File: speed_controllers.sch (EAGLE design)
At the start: 18 parts

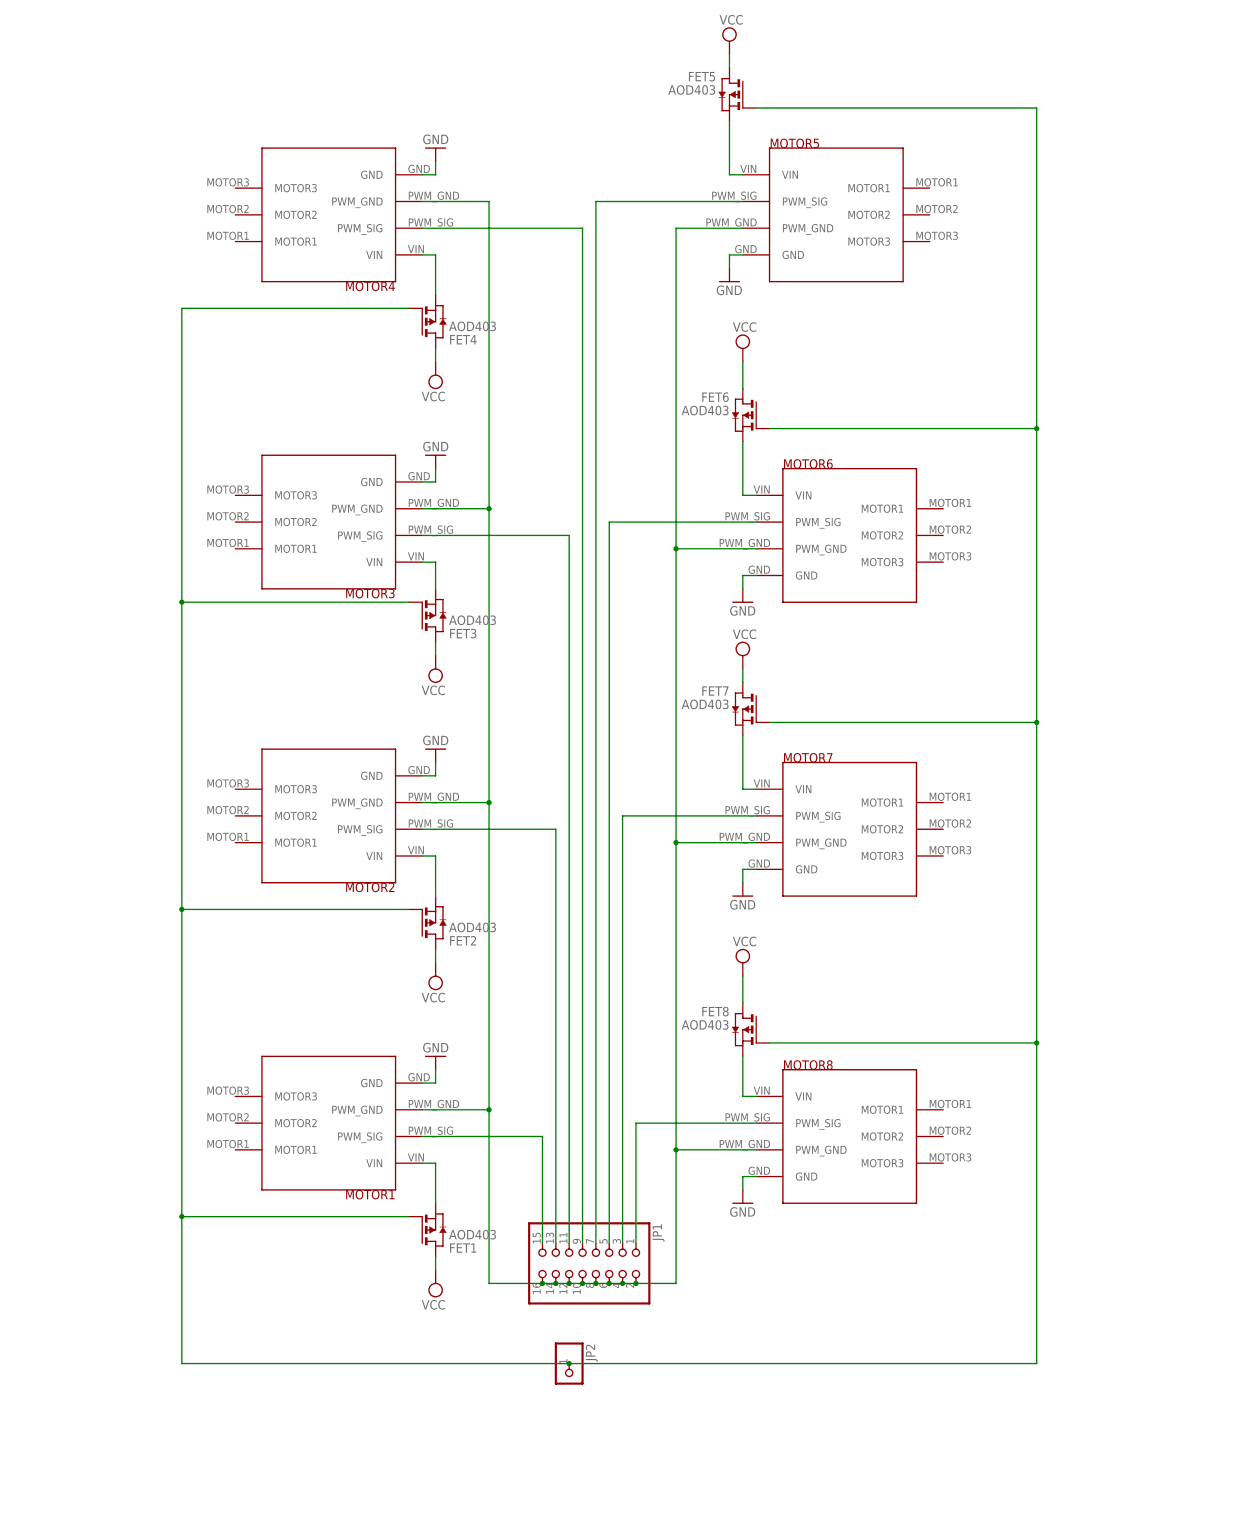
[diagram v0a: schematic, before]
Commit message: Redone ESC boards
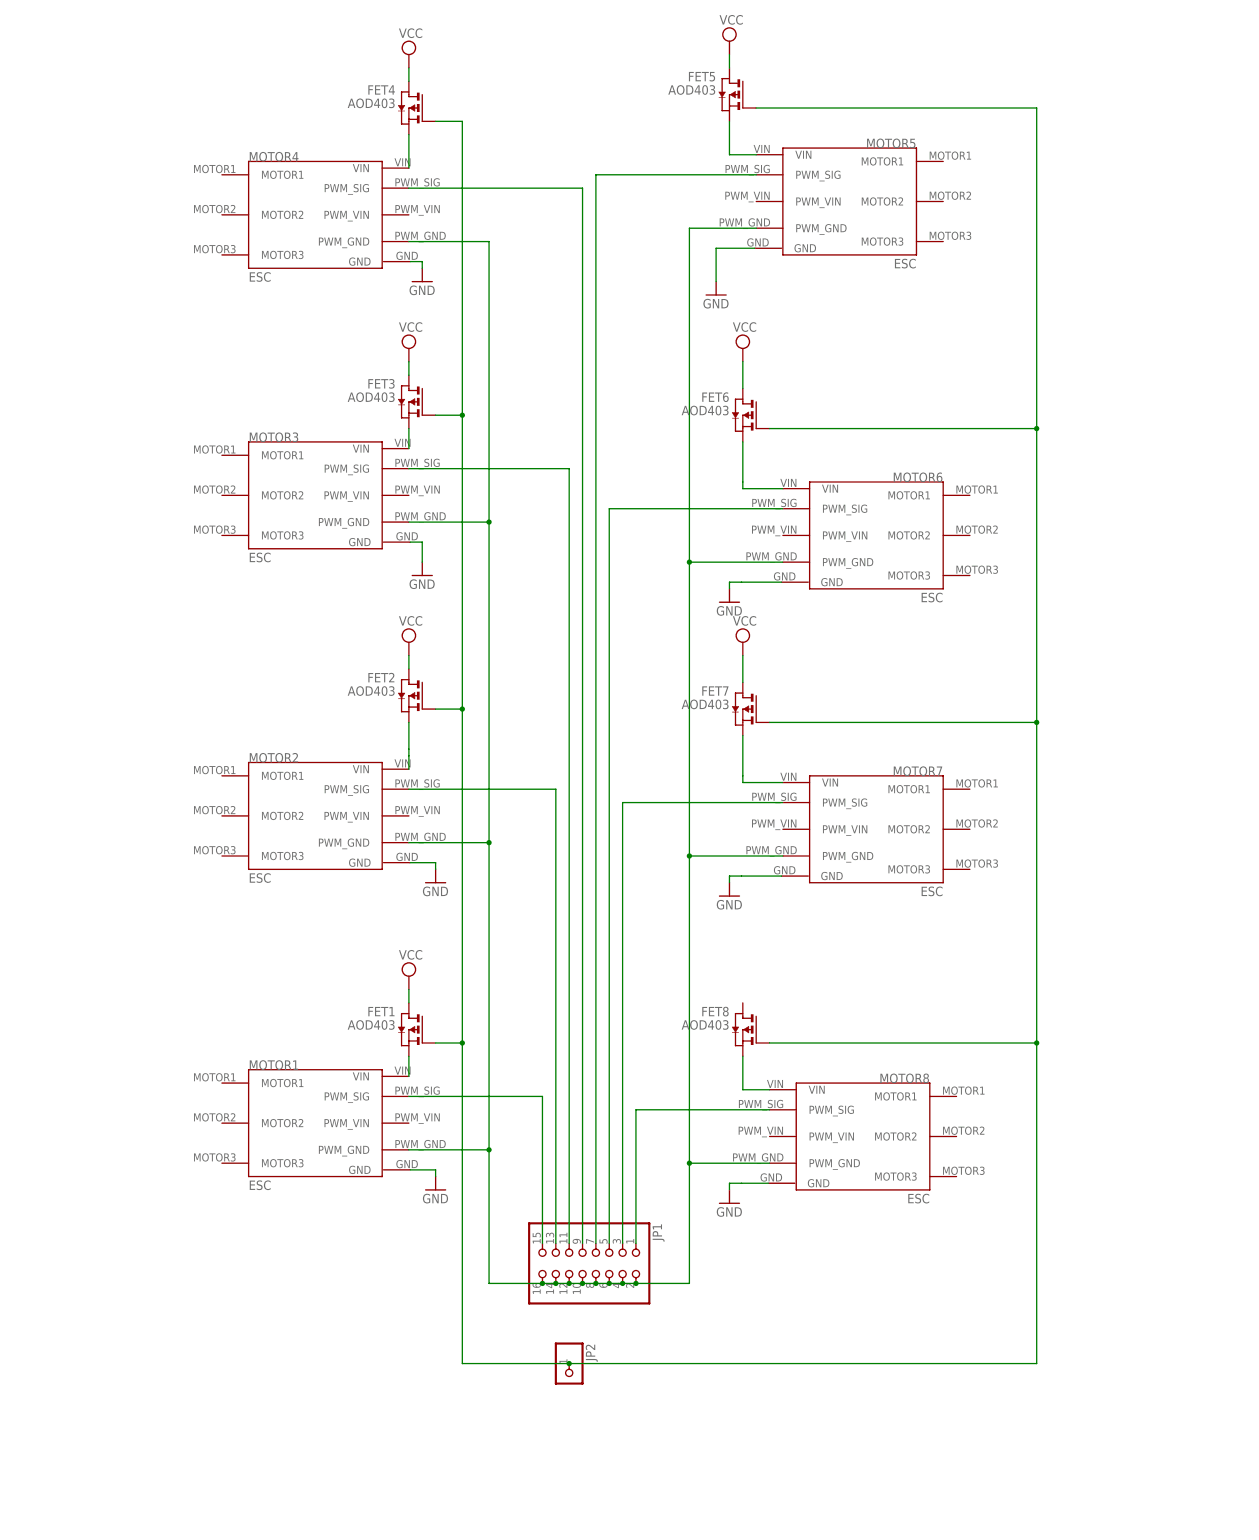
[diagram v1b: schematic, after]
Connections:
- net VCC: no longer FET8.D
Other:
- moved on the sheet: FET1, FET2, FET3, FET4

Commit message: Fixed everything in issue Redone ESC boards #2
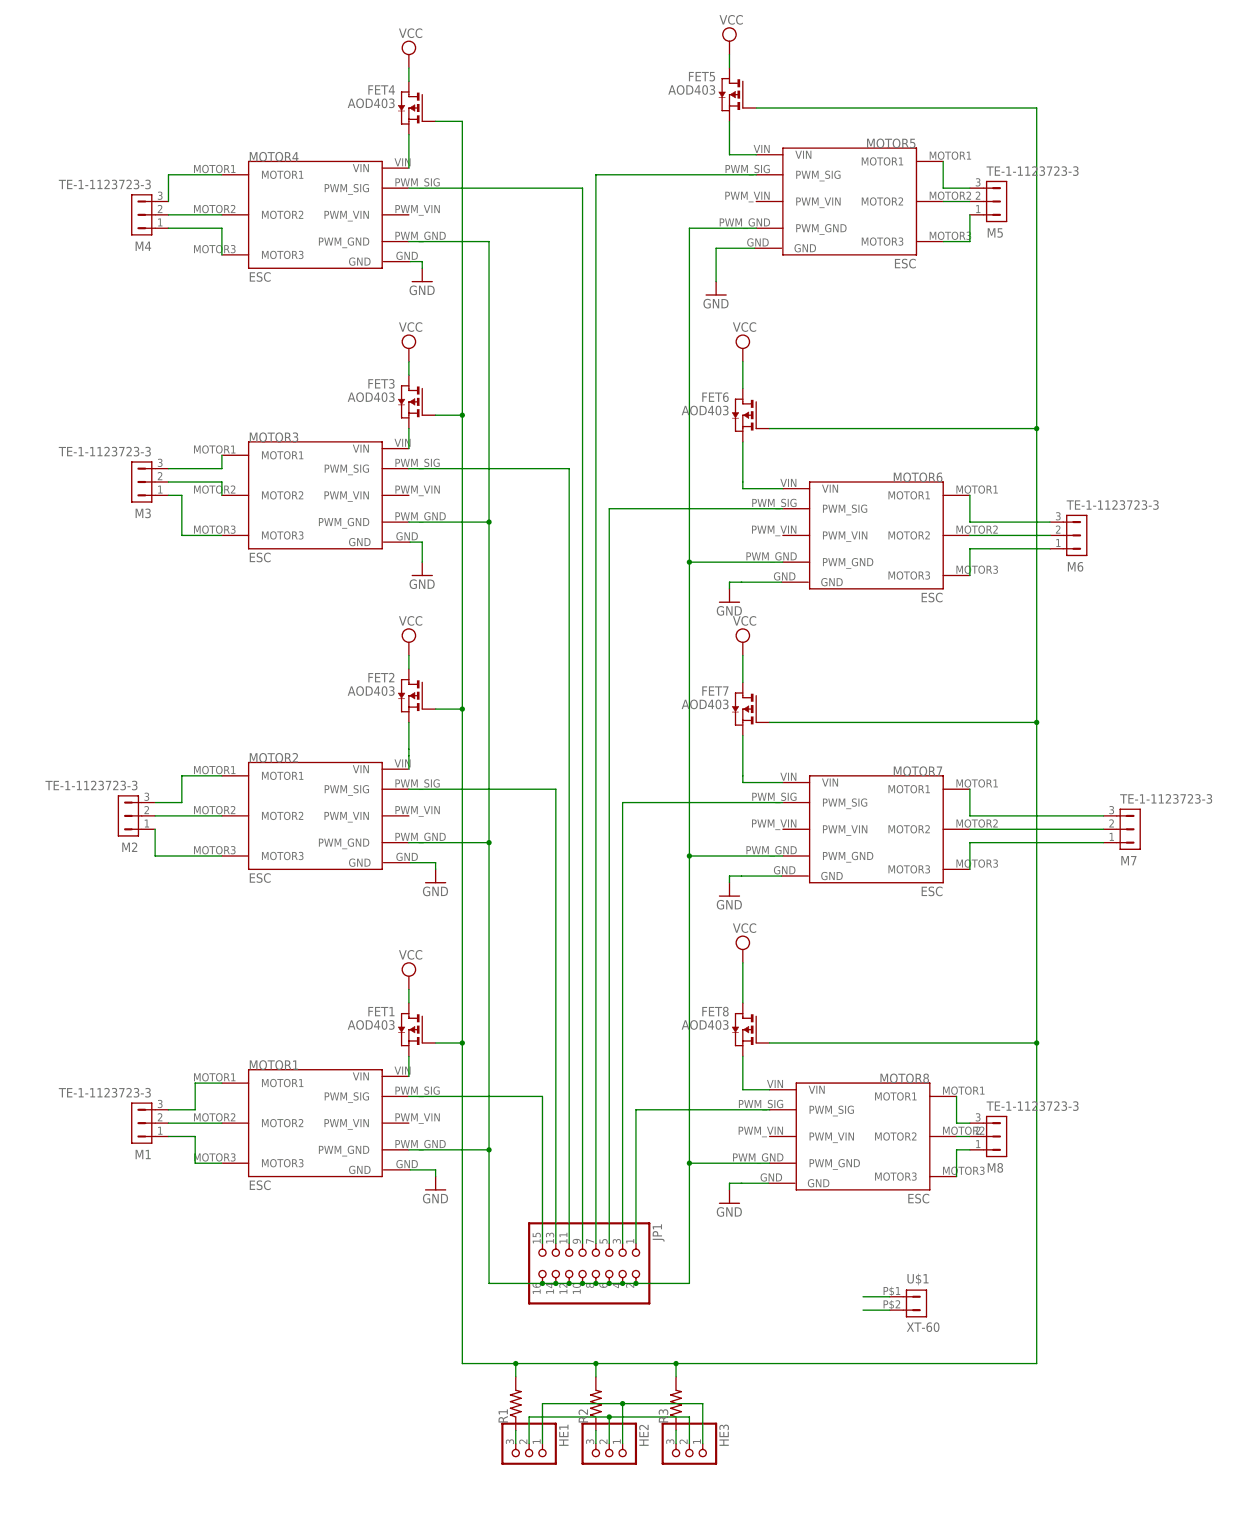
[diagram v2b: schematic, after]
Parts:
- removed JP2: (no value), auv:PINHD-1X1
- added HE1, HE2, HE3: (no value), auv:PINHD-1X3
- added M1, M2, M3, M4, M5, M6, M7, M8: TE-1-1123723-3, auv:TE-1-1123723-3
- added R1, R2, R3: (no value), auv:R-US_R0603
- added U$1: XT-60, auv:XT-60
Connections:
- net N$1 renamed SIG_6
- net N$10 renamed SIG_3
- net N$11 renamed SIG_2
- net N$12 renamed SIG_7
- net N$13 renamed SIG_8
- net N$14 renamed SIG_1
- net N$15 renamed VIN_2
- net N$16 renamed VIN3
- net N$17 renamed VIN_4
- net N$18 renamed VIN_8
- net N$2 renamed PWM_GND
- net N$3 renamed VIN_1
- net N$4 renamed SIG_5
- net N$5 renamed VIN_5
- net N$6 renamed SIG_4
- net N$8 renamed VIN_7
- net N$9 renamed VIN_6
- removed net N$20: FET1.G, FET2.G, FET3.G, FET4.G, FET5.G, FET6.G, FET7.G, FET8.G, JP2.1
- new net FET_G: FET1.G, FET2.G, FET3.G, FET4.G, FET5.G, FET6.G, FET7.G, FET8.G, R1.2, R2.2, R3.2
- new net M1_1: M1.1, MOTOR1.MOTOR3
- new net M1_2: M1.2, MOTOR1.MOTOR2
- new net M1_3: M1.3, MOTOR1.MOTOR1
- new net M2_1: M2.1, MOTOR2.MOTOR3
- new net M2_2: M2.2, MOTOR2.MOTOR2
- new net M2_3: M2.3, MOTOR2.MOTOR1
- new net M3_1: M3.1, MOTOR3.MOTOR3
- new net M3_2: M3.2, MOTOR3.MOTOR2
- new net M3_3: M3.3, MOTOR3.MOTOR1
- new net M4_1: M4.1, MOTOR4.MOTOR3
- new net M4_2: M4.2, MOTOR4.MOTOR2
- new net M4_3: M4.3, MOTOR4.MOTOR1
- new net M5_1: M5.1, MOTOR5.MOTOR3
- new net M5_2: M5.2, MOTOR5.MOTOR2
- new net M5_3: M5.3, MOTOR5.MOTOR1
- new net M6_1: M6.1, MOTOR6.MOTOR3
- new net M6_2: M6.2, MOTOR6.MOTOR2
- new net M6_3: M6.3, MOTOR6.MOTOR1
- new net M7_1: M7.1, MOTOR7.MOTOR3
- new net M7_2: M7.2, MOTOR7.MOTOR2
- new net M7_3: M7.3, MOTOR7.MOTOR1
- new net M8_1: M8.1, MOTOR8.MOTOR3
- new net M8_2: M8.2, MOTOR8.MOTOR2
- new net M8_3: M8.3, MOTOR8.MOTOR1
- new net N$4: HE1.3, R1.1
- new net N$5: HE2.3, R2.1
- new net N$6: HE3.3, R3.1
- net GND: now also HE1.2, HE2.2, HE3.2, U$1.2
- net VCC: now also FET8.D, HE1.1, HE2.1, HE3.1, U$1.1

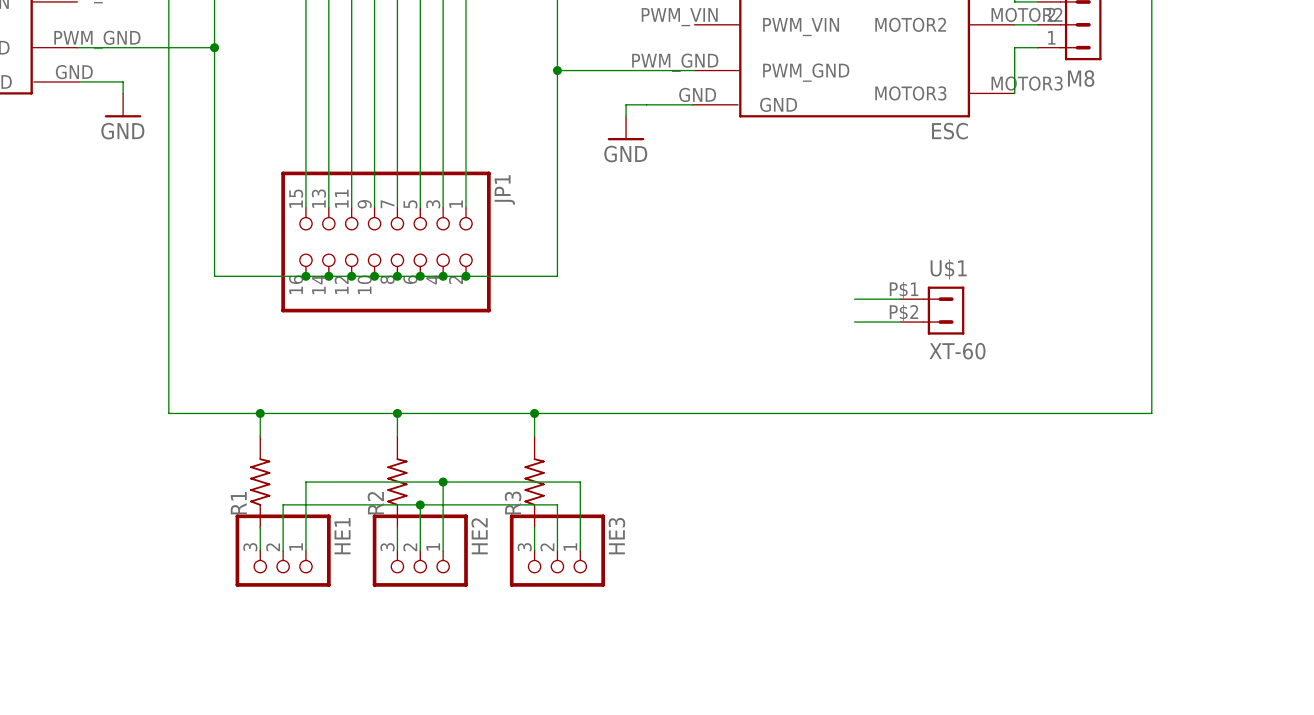
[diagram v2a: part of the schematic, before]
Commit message: Added Optocoupler and Hall effect sensors
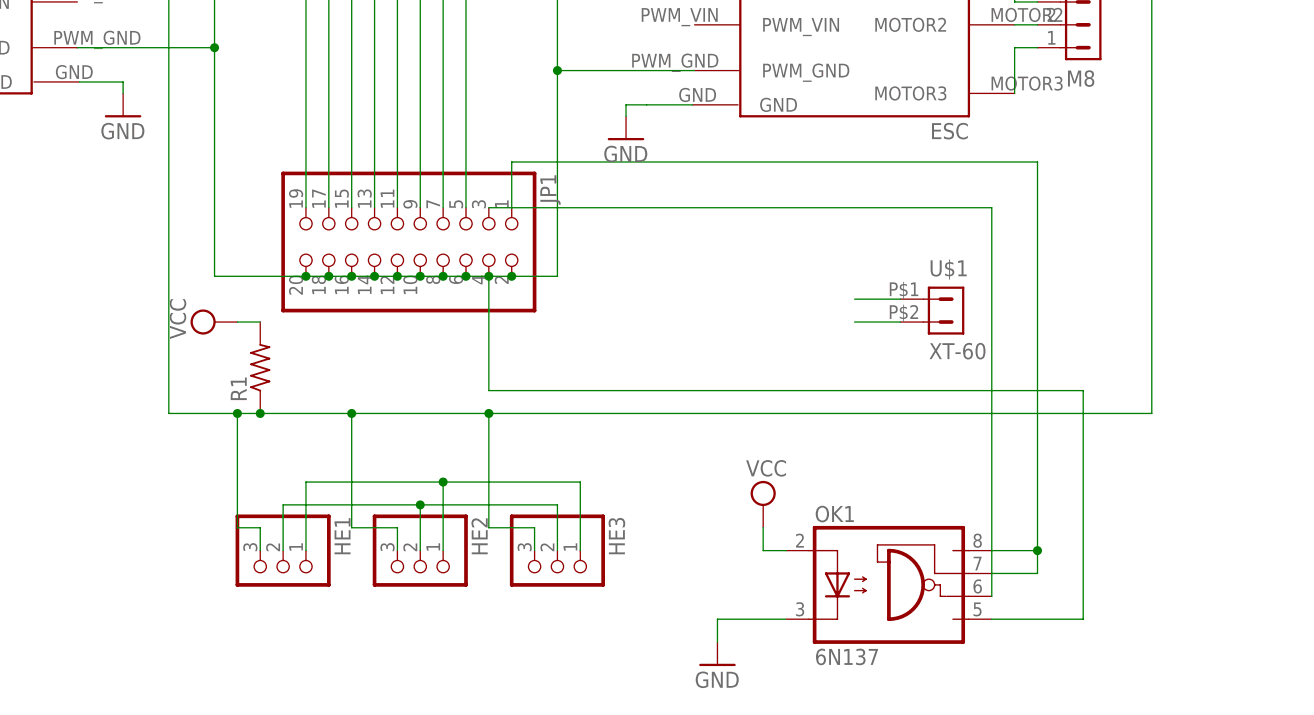
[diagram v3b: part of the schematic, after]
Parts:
- removed R2, R3: (no value), auv:R-US_R0603
- added OK1: 6N137, auv:6N137
- JP1: device auv:PINHD-2X8 -> auv:PINHD-2X10
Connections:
- removed net N$6: HE3.3, R3.1
- net FET_G: now also HE1.3, HE2.3, HE3.3, R1.1; no longer R1.2, R2.2, R3.2
- net GND: now also OK1.C
- net N$4: now also JP1.1, OK1.VCC, OK1.VE; no longer HE1.3, R1.1
- net N$5: now also JP1.3, OK1.VO; no longer HE2.3, R2.1
- net PWM_GND: now also JP1.18, JP1.20, OK1.GND
- net SIG_1: now also JP1.19; no longer JP1.15
- net SIG_2: now also JP1.17; no longer JP1.13
- net SIG_3: now also JP1.15; no longer JP1.11
- net SIG_4: now also JP1.13; no longer JP1.9
- net SIG_5: now also JP1.11; no longer JP1.7
- net SIG_6: now also JP1.9; no longer JP1.5
- net SIG_7: now also JP1.7; no longer JP1.3
- net SIG_8: now also JP1.5; no longer JP1.1
- net VCC: now also OK1.A, R1.2
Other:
- moved on the sheet: R1

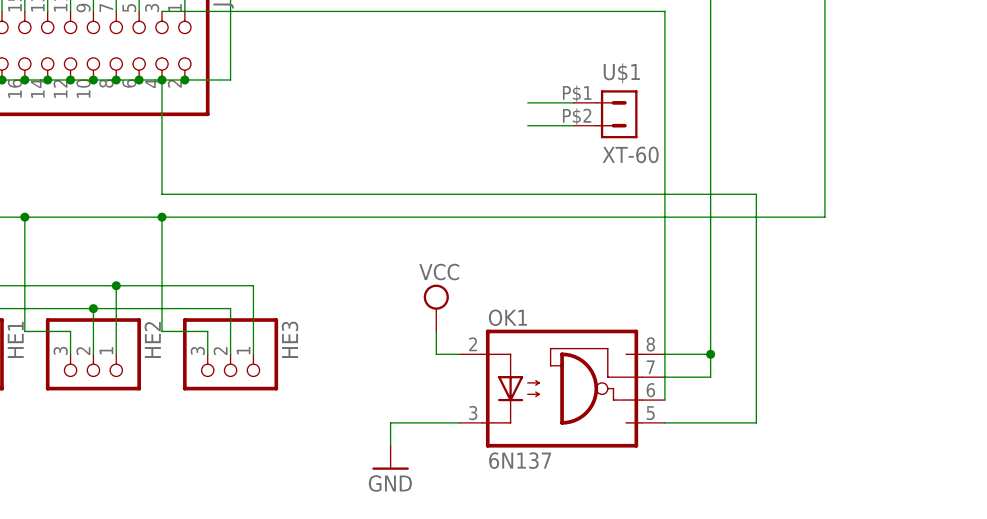
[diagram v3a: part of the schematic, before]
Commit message: Rewired optocontroller
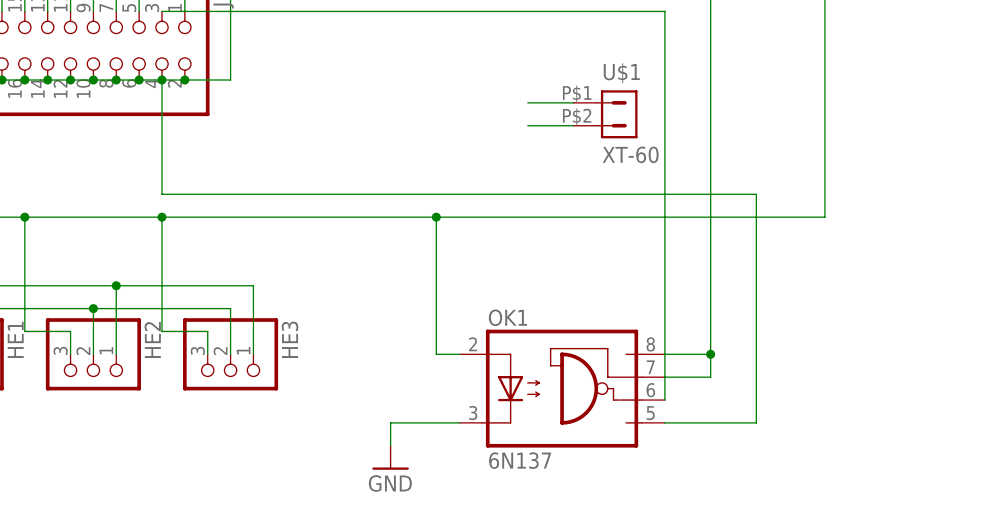
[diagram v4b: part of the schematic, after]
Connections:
- net FET_G: now also OK1.A
- net VCC: no longer OK1.A
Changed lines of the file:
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@@
 <part name="SUPPLY9" library="auv" deviceset="VCC" device=""/>
 <part name="OK1" library="auv" deviceset="6N137" device=""/>
-<part name="SUPPLY10" library="auv" deviceset="VCC" device=""/>
 <part name="GND9" library="auv" deviceset="GND" device=""/>
 <part name="JP1" library="auv" deviceset="PINHD-2X10" device=""/>
@@
 <instance part="SUPPLY9" gate="G$1" x="12.7" y="-81.28" rot="R90"/>
 <instance part="OK1" gate="A" x="88.9" y="-111.76"/>
-<instance part="SUPPLY10" gate="G$1" x="73.66" y="-101.6"/>
 <instance part="GND9" gate="1" x="68.58" y="-119.38"/>
 <instance part="JP1" gate="A" x="35.56" y="-71.12" rot="R270"/>
@@
 <wire x1="17.78" y1="-81.28" x2="15.24" y2="-81.28" width="0.1524" layer="91"/>
 </segment>
-<segment>
-<pinref part="OK1" gate="A" pin="A"/>
-<pinref part="SUPPLY10" gate="G$1" pin="VCC"/>
-<wire x1="76.2" y1="-106.68" x2="73.66" y2="-106.68" width="0.1524" layer="91"/>
-<wire x1="73.66" y1="-106.68" x2="73.66" y2="-104.14" width="0.1524" layer="91"/>
-</segment>
 </net>
 <net name="FET_G" class="0">
@@
 <wire x1="116.84" y1="30.48" x2="116.84" y2="-30.48" width="0.1524" layer="91"/>
 <wire x1="116.84" y1="-30.48" x2="116.84" y2="-91.44" width="0.1524" layer="91"/>
-<wire x1="116.84" y1="-91.44" x2="43.18" y2="-91.44" width="0.1524" layer="91"/>
+<wire x1="116.84" y1="-91.44" x2="73.66" y2="-91.44" width="0.1524" layer="91"/>
 <pinref part="FET7" gate="G$1" pin="G"/>
+<wire x1="73.66" y1="-91.44" x2="43.18" y2="-91.44" width="0.1524" layer="91"/>
 <wire x1="43.18" y1="-91.44" x2="27.94" y2="-91.44" width="0.1524" layer="91"/>
 <wire x1="27.94" y1="-91.44" x2="17.78" y2="-91.44" width="0.1524" layer="91"/>
@@
 <pinref part="R1" gate="G$1" pin="1"/>
 <junction x="17.78" y="-91.44"/>
+<pinref part="OK1" gate="A" pin="A"/>
+<wire x1="76.2" y1="-106.68" x2="73.66" y2="-106.68" width="0.1524" layer="91"/>
+<wire x1="73.66" y1="-106.68" x2="73.66" y2="-91.44" width="0.1524" layer="91"/>
+<junction x="73.66" y="-91.44"/>
 </segment>
 </net>
